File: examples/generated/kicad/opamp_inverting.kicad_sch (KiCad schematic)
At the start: 7 parts

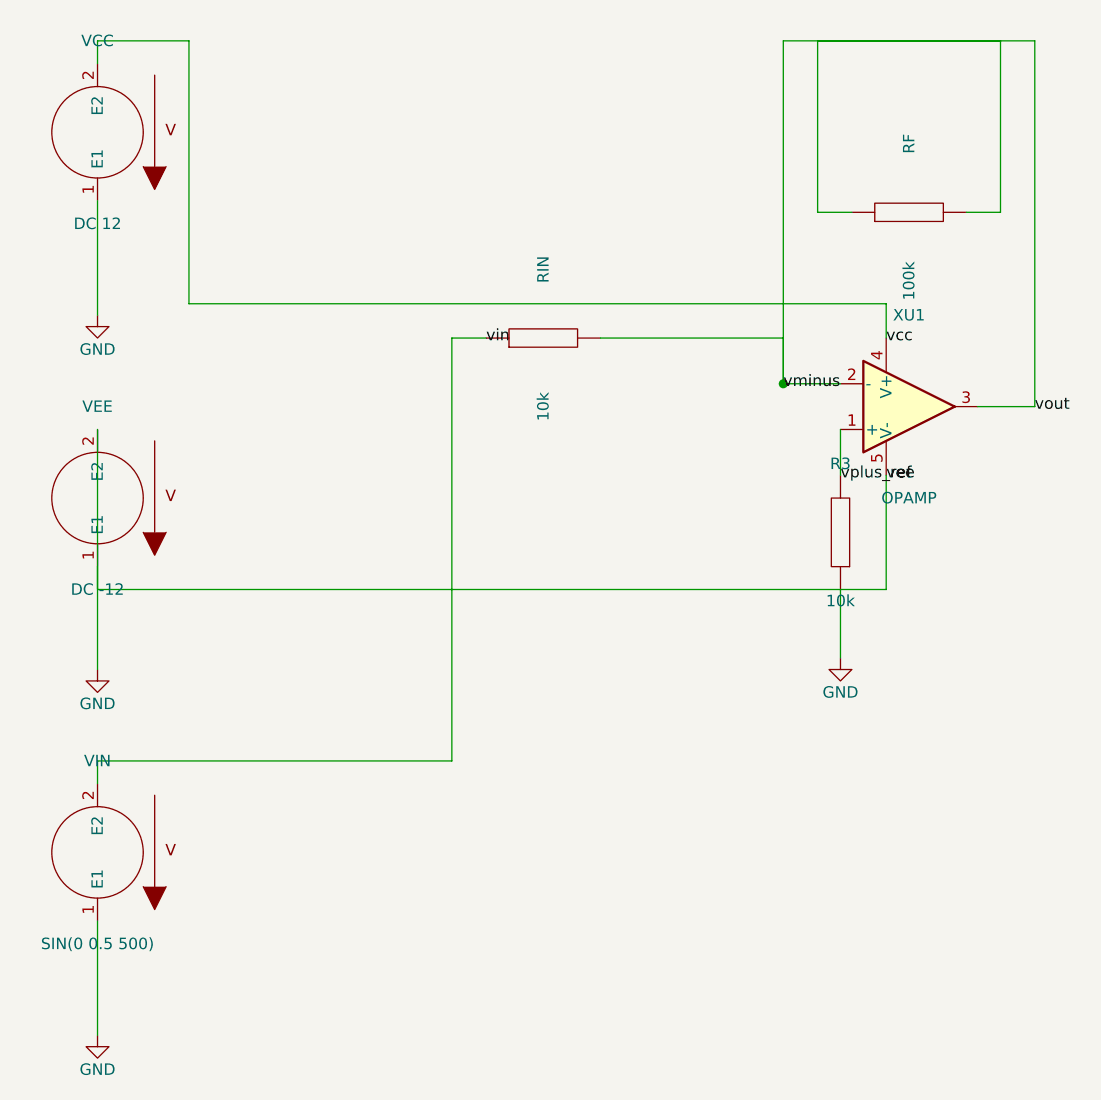
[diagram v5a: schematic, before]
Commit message: Attempt to fix non-inverting op-amp connectivity issues.
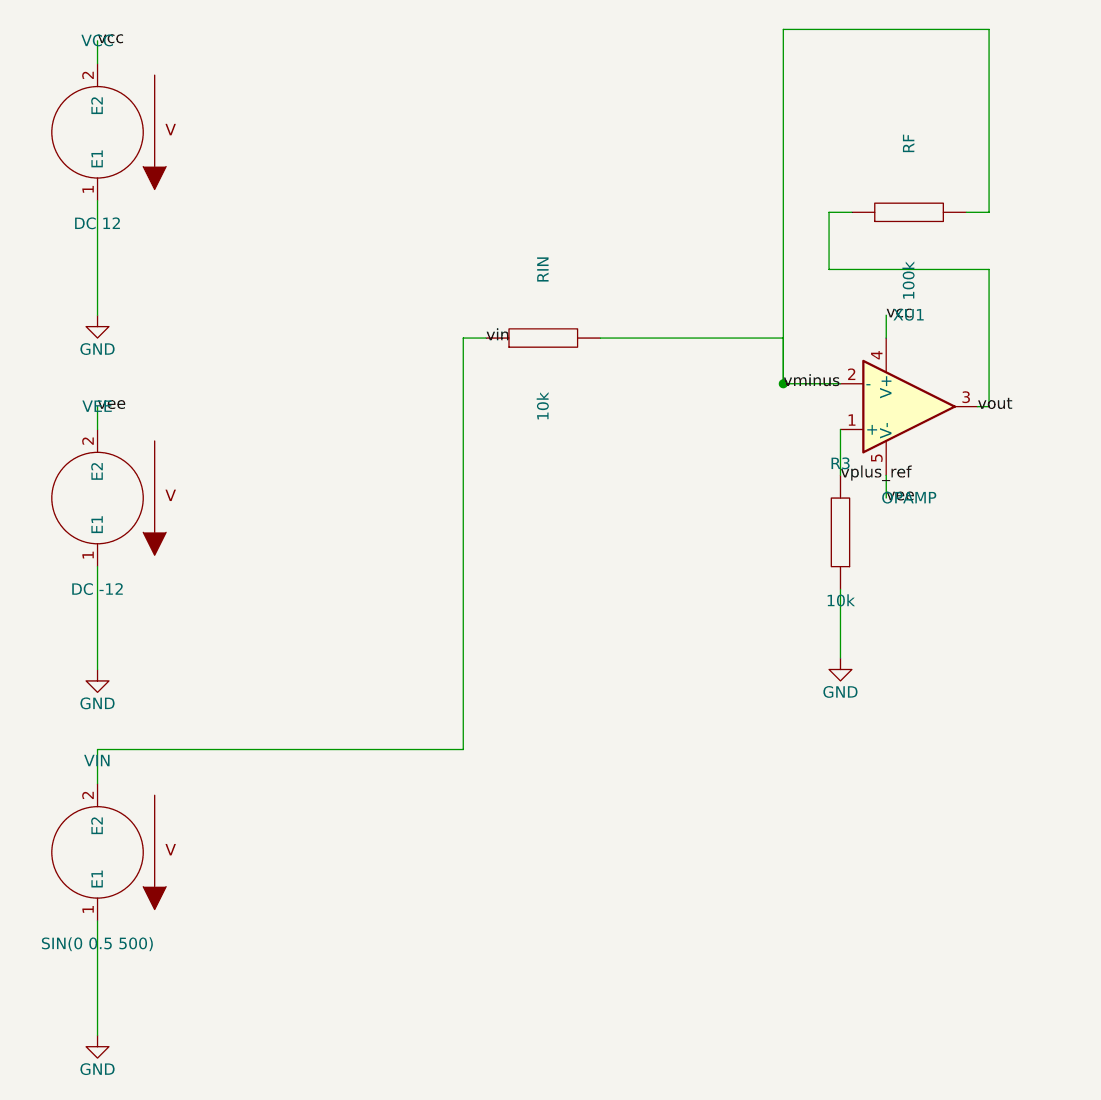
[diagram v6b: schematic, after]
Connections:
- net GND: no longer VEE.2 (E2), XU1.5 (V-)
- net vminus: no longer RF.1, XU1.3
- new net vee: VEE.2 (E2), XU1.5 (V-)
- new net vout: RF.1, XU1.3
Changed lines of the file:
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@@
     )
+  )
+  (label "vcc" (at 167.64 80.01 0)
+    (effects (font (size 1.27 1.27)))
+  )
+  (label "vcc" (at 80.01 49.53 0)
+    (effects (font (size 1.27 1.27)))
+  )
+  (label "vee" (at 167.64 100.33 0)
+    (effects (font (size 1.27 1.27)))
+  )
+  (label "vee" (at 80.01 90.17 0)
+    (effects (font (size 1.27 1.27)))
   )
   (label "vin" (at 123.19 82.55 0)
@@
     (effects (font (size 1.27 1.27)))
   )
-  (label "vout" (at 184.15 90.17 0)
+  (label "vout" (at 177.80 90.17 0)
     (effects (font (size 1.27 1.27)))
   )
-  (label "vcc" (at 167.64 82.55 0)
-    (effects (font (size 1.27 1.27)))
+  (wire (pts (xy 167.64 82.55) (xy 167.64 80.01))
+    (stroke (width 0) (type solid) (color 0 0 0 0))
   )
-  (label "vee" (at 167.64 97.79 0)
-    (effects (font (size 1.27 1.27)))
+  (wire (pts (xy 80.01 52.07) (xy 80.01 49.53))
+    (stroke (width 0) (type solid) (color 0 0 0 0))
+  )
+  (wire (pts (xy 167.64 97.79) (xy 167.64 100.33))
+    (stroke (width 0) (type solid) (color 0 0 0 0))
+  )
+  (wire (pts (xy 80.01 92.71) (xy 80.01 90.17))
+    (stroke (width 0) (type solid) (color 0 0 0 0))
   )
   (wire (pts (xy 80.01 67.31) (xy 80.01 80.01))
@@
     (stroke (width 0) (type solid) (color 0 0 0 0))
   )
-  (wire (pts (xy 80.01 132.08) (xy 80.01 129.54))
+  (wire (pts (xy 80.01 132.08) (xy 80.01 128.27))
     (stroke (width 0) (type solid) (color 0 0 0 0))
   )
-  (wire (pts (xy 80.01 129.54) (xy 119.38 129.54))
+  (wire (pts (xy 80.01 128.27) (xy 120.65 128.27))
     (stroke (width 0) (type solid) (color 0 0 0 0))
   )
-  (wire (pts (xy 119.38 129.54) (xy 119.38 82.55))
+  (wire (pts (xy 120.65 128.27) (xy 120.65 82.55))
     (stroke (width 0) (type solid) (color 0 0 0 0))
   )
-  (wire (pts (xy 119.38 82.55) (xy 123.19 82.55))
+  (wire (pts (xy 120.65 82.55) (xy 123.19 82.55))
     (stroke (width 0) (type solid) (color 0 0 0 0))
   )
@@
     (stroke (width 0) (type solid) (color 0 0 0 0))
   )
-  (wire (pts (xy 176.53 68.58) (xy 180.34 68.58))
+  (wire (pts (xy 176.53 68.58) (xy 179.07 68.58))
     (stroke (width 0) (type solid) (color 0 0 0 0))
   )
-  (wire (pts (xy 180.34 68.58) (xy 180.34 49.53))
+  (wire (pts (xy 179.07 68.58) (xy 179.07 48.26))
     (stroke (width 0) (type solid) (color 0 0 0 0))
   )
-  (wire (pts (xy 180.34 49.53) (xy 156.21 49.53))
+  (wire (pts (xy 179.07 48.26) (xy 156.21 48.26))
     (stroke (width 0) (type solid) (color 0 0 0 0))
   )
-  (wire (pts (xy 156.21 49.53) (xy 156.21 87.63))
+  (wire (pts (xy 156.21 48.26) (xy 156.21 87.63))
     (stroke (width 0) (type solid) (color 0 0 0 0))
   )
-  (wire (pts (xy 177.80 90.17) (xy 184.15 90.17))
+  (wire (pts (xy 177.80 90.17) (xy 179.07 90.17))
     (stroke (width 0) (type solid) (color 0 0 0 0))
   )
-  (wire (pts (xy 163.83 68.58) (xy 160.02 68.58))
+  (wire (pts (xy 179.07 90.17) (xy 179.07 74.93))
     (stroke (width 0) (type solid) (color 0 0 0 0))
   )
-  (wire (pts (xy 160.02 68.58) (xy 160.02 49.53))
+  (wire (pts (xy 179.07 74.93) (xy 161.29 74.93))
     (stroke (width 0) (type solid) (color 0 0 0 0))
   )
-  (wire (pts (xy 160.02 49.53) (xy 184.15 49.53))
+  (wire (pts (xy 161.29 74.93) (xy 161.29 68.58))
     (stroke (width 0) (type solid) (color 0 0 0 0))
   )
-  (wire (pts (xy 184.15 49.53) (xy 184.15 90.17))
+  (wire (pts (xy 161.29 68.58) (xy 163.83 68.58))
     (stroke (width 0) (type solid) (color 0 0 0 0))
   )
-  (wire (pts (xy 167.64 82.55) (xy 167.64 78.74))
-    (stroke (width 0) (type solid) (color 0 0 0 0))
-  )
-  (wire (pts (xy 167.64 78.74) (xy 90.17 78.74))
-    (stroke (width 0) (type solid) (color 0 0 0 0))
-  )
-  (wire (pts (xy 90.17 78.74) (xy 90.17 49.53))
-    (stroke (width 0) (type solid) (color 0 0 0 0))
-  )
-  (wire (pts (xy 90.17 49.53) (xy 80.01 49.53))
-    (stroke (width 0) (type solid) (color 0 0 0 0))
-  )
-  (wire (pts (xy 80.01 49.53) (xy 80.01 52.07))
-    (stroke (width 0) (type solid) (color 0 0 0 0))
-  )
-  (wire (pts (xy 167.64 97.79) (xy 167.64 110.49))
-    (stroke (width 0) (type solid) (color 0 0 0 0))
-  )
-  (wire (pts (xy 167.64 110.49) (xy 80.01 110.49))
-    (stroke (width 0) (type solid) (color 0 0 0 0))
-  )
-  (wire (pts (xy 80.01 110.49) (xy 80.01 92.71))
-    (stroke (width 0) (type solid) (color 0 0 0 0))
-  )

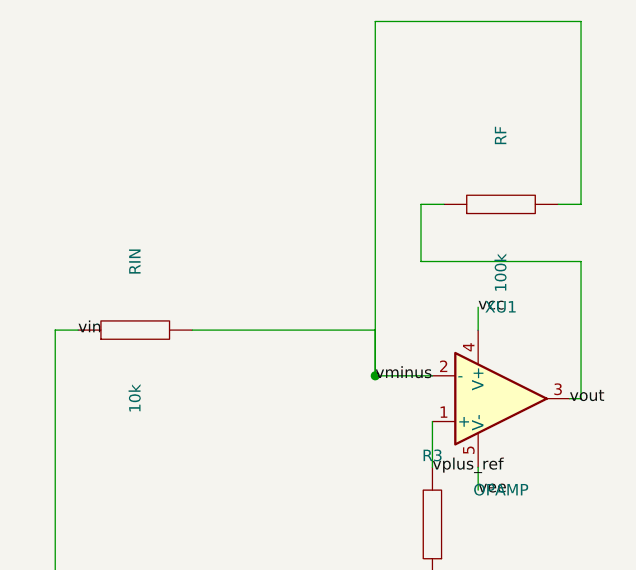
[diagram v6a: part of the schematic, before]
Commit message: Attempt to fix non-inverting op-amp kinked wiring.
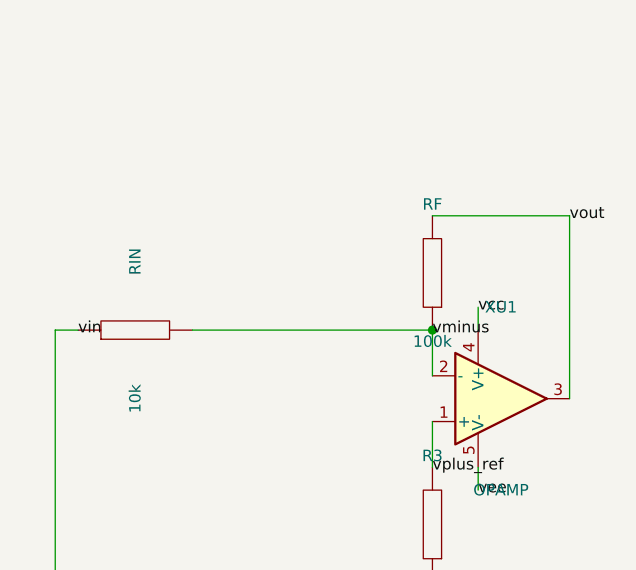
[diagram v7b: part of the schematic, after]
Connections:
- net vminus: now also RF.1; no longer RF.2
- net vout: now also RF.2; no longer RF.1
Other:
- moved on the sheet: RF
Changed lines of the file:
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@@
     )
   )
-  (symbol (lib_id "R") (at 170.18 68.58 90) (unit 1)
-    (in_bom yes) (on_board yes)
-    (property "Reference" "RF" (at 170.18 60.96 0)
-      (effects (font (size 1.27 1.27)))
-    )
-    (property "Value" "100k" (at 170.18 76.2 0)
+  (symbol (lib_id "R") (at 162.56 76.20 180) (unit 1)
+    (in_bom yes) (on_board yes)
+    (property "Reference" "RF" (at 162.56 68.58 0)
+      (effects (font (size 1.27 1.27)))
+    )
+    (property "Value" "100k" (at 162.56 83.82 0)
       (effects (font (size 1.27 1.27)))
     )
@@
     (effects (font (size 1.27 1.27)))
   )
-  (label "vminus" (at 156.21 87.63 0)
-    (effects (font (size 1.27 1.27)))
-  )
-  (label "vout" (at 177.80 90.17 0)
+  (label "vminus" (at 162.56 82.55 0)
+    (effects (font (size 1.27 1.27)))
+  )
+  (label "vout" (at 177.80 69.85 0)
     (effects (font (size 1.27 1.27)))
   )
@@
     (stroke (width 0) (type solid) (color 0 0 0 0))
   )
-  (wire (pts (xy 135.89 82.55) (xy 156.21 82.55))
-    (stroke (width 0) (type solid) (color 0 0 0 0))
-  )
-  (wire (pts (xy 156.21 82.55) (xy 156.21 87.63))
-    (stroke (width 0) (type solid) (color 0 0 0 0))
-  )
-  (wire (pts (xy 162.56 87.63) (xy 156.21 87.63))
-    (stroke (width 0) (type solid) (color 0 0 0 0))
-  )
-  (wire (pts (xy 176.53 68.58) (xy 179.07 68.58))
-    (stroke (width 0) (type solid) (color 0 0 0 0))
-  )
-  (wire (pts (xy 179.07 68.58) (xy 179.07 48.26))
-    (stroke (width 0) (type solid) (color 0 0 0 0))
-  )
-  (wire (pts (xy 179.07 48.26) (xy 156.21 48.26))
-    (stroke (width 0) (type solid) (color 0 0 0 0))
-  )
-  (wire (pts (xy 156.21 48.26) (xy 156.21 87.63))
-    (stroke (width 0) (type solid) (color 0 0 0 0))
-  )
-  (wire (pts (xy 177.80 90.17) (xy 179.07 90.17))
-    (stroke (width 0) (type solid) (color 0 0 0 0))
-  )
-  (wire (pts (xy 179.07 90.17) (xy 179.07 74.93))
-    (stroke (width 0) (type solid) (color 0 0 0 0))
-  )
-  (wire (pts (xy 179.07 74.93) (xy 161.29 74.93))
-    (stroke (width 0) (type solid) (color 0 0 0 0))
-  )
-  (wire (pts (xy 161.29 74.93) (xy 161.29 68.58))
-    (stroke (width 0) (type solid) (color 0 0 0 0))
-  )
-  (wire (pts (xy 161.29 68.58) (xy 163.83 68.58))
-    (stroke (width 0) (type solid) (color 0 0 0 0))
-  )
-  (junction (at 156.21 87.63) (diameter 1.016) (color 0 0 0 0))
+  (wire (pts (xy 135.89 82.55) (xy 162.56 82.55))
+    (stroke (width 0) (type solid) (color 0 0 0 0))
+  )
+  (wire (pts (xy 162.56 87.63) (xy 162.56 82.55))
+    (stroke (width 0) (type solid) (color 0 0 0 0))
+  )
+  (wire (pts (xy 177.80 90.17) (xy 177.80 69.85))
+    (stroke (width 0) (type solid) (color 0 0 0 0))
+  )
+  (wire (pts (xy 162.56 69.85) (xy 177.80 69.85))
+    (stroke (width 0) (type solid) (color 0 0 0 0))
+  )
+  (junction (at 162.56 82.55) (diameter 1.016) (color 0 0 0 0))
   (sheet_instances
     (path "/" (page "1"))
